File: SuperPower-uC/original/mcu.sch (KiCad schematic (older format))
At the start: 43 parts, among them J7 mcu_pinout, J8 mcu_pinout, Q7 S8050, Q8 S8050, U6 CP2102N-A01-GQFN28, U7 ESP32-WROOM32

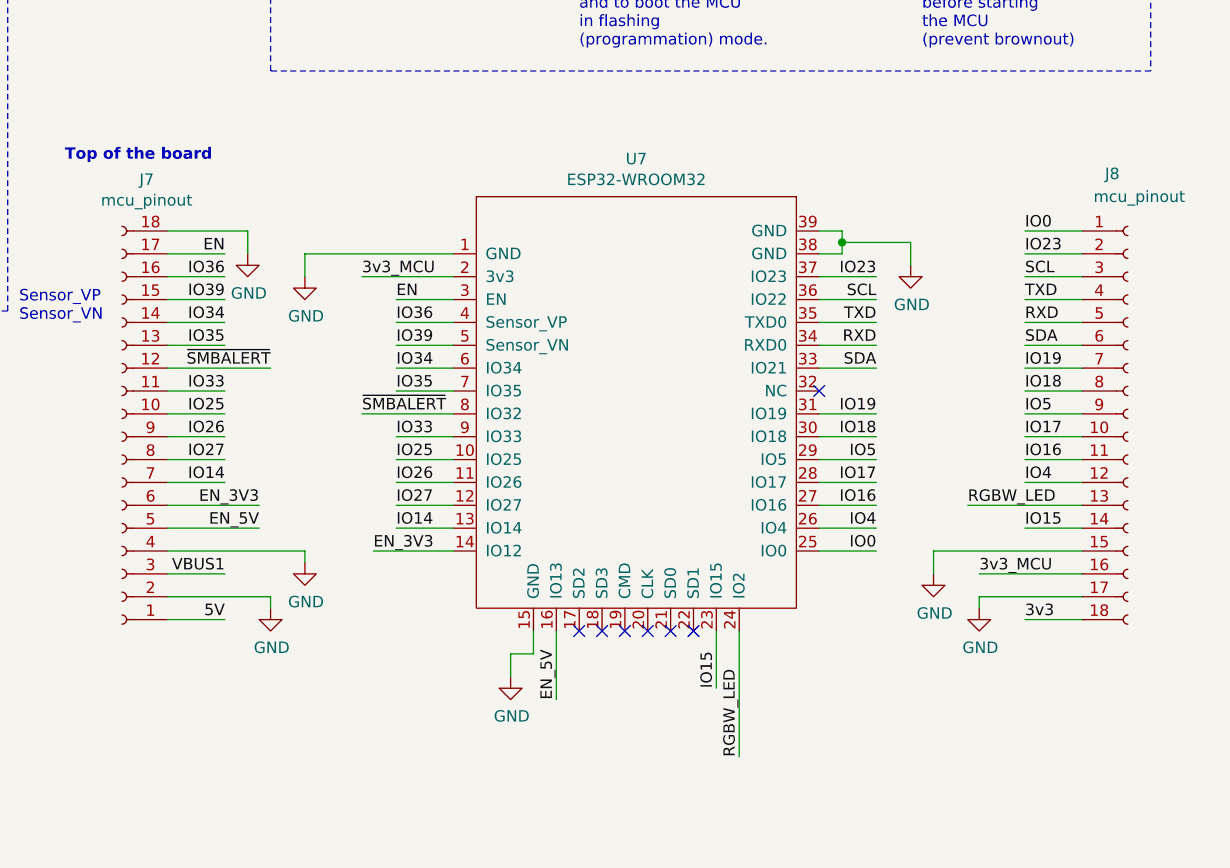
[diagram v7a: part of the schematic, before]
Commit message: Added additional 5+ amd 3.3+ - swapped VBUS to other connector
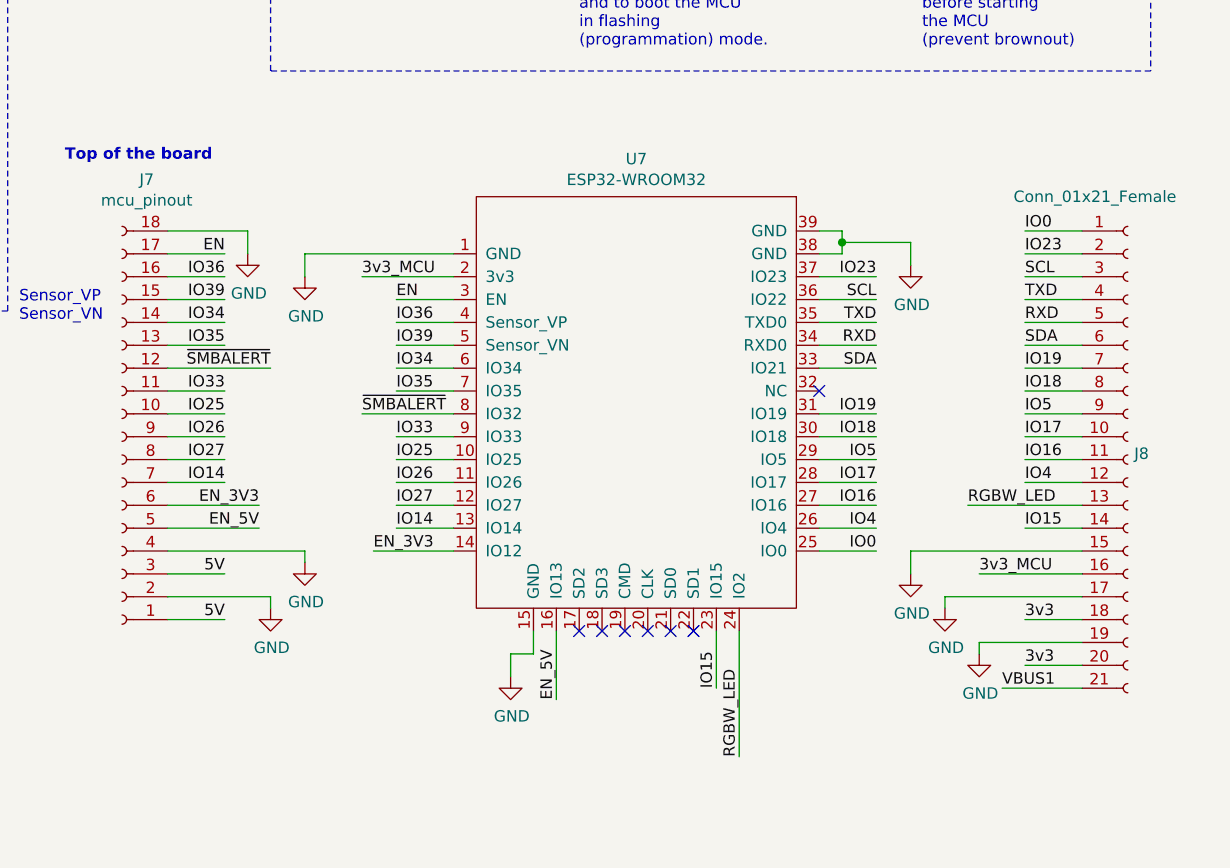
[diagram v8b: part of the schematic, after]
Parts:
- removed J8: mcu_pinout, Connector_PinSocket_2.54mm:PinSocket_1x18_P2.54mm_Vertical, symbol Connector:Conn_01x18_Female
- added J8: Conn_01x21_Female, Connector_PinSocket_2.54mm:PinSocket_1x21_P2.54mm_Vertical, symbol Connector:Conn_01x21_Female
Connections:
- net 3v3: now also J8.18 (Pin_18), J8.20 (Pin_20)
- net 3v3_MCU: now also J8.16 (Pin_16)
- net 5V: now also J7.3 (Pin_3)
- net GND: now also J8.15 (Pin_15), J8.17 (Pin_17), J8.19 (Pin_19)
- net IO0: now also J8.1 (Pin_1)
- net IO15: now also J8.14 (Pin_14)
- net IO16: now also J8.11 (Pin_11)
- net IO17: now also J8.10 (Pin_10)
- net IO18: now also J8.8 (Pin_8)
- net IO19: now also J8.7 (Pin_7)
- net IO23: now also J8.2 (Pin_2)
- net IO4: now also J8.12 (Pin_12)
- net IO5: now also J8.9 (Pin_9)
- net RGBW_LED: now also J8.13 (Pin_13)
- net RXD: now also J8.5 (Pin_5)
- net SCL: now also J8.3 (Pin_3)
- net SDA: now also J8.6 (Pin_6)
- net TXD: now also J8.4 (Pin_4)
- net VBUS1: now also J8.21 (Pin_21); no longer J7.3 (Pin_3)
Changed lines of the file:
@@
 L power:GND #PWR053
 U 1 1 5F8B01AA
-P 9750 5600
-F 0 "#PWR053" H 9750 5350 50  0001 C CNN
-F 1 "GND" H 9755 5427 50  0000 C CNN
-F 2 "" H 9750 5600 50  0001 C CNN
-F 3 "" H 9750 5600 50  0001 C CNN
-	1    9750 5600
-	1    0    0    -1
-$EndComp
-Wire Wire Line
-	9750 5600 9750 5500
+P 9650 5600
+F 0 "#PWR053" H 9650 5350 50  0001 C CNN
+F 1 "GND" H 9655 5427 50  0000 C CNN
+F 2 "" H 9650 5600 50  0001 C CNN
+F 3 "" H 9650 5600 50  0001 C CNN
+	1    9650 5600
+	1    0    0    -1
+$EndComp
 $Comp
 L power:PWR_FLAG #FLG?
@@
 Wire Wire Line
 	6400 5600 6650 5600
-Text Label 6650 5600 2    50   ~ 0
+Text Label 10050 6100 0    50   ~ 0
 VBUS1
 $Comp
@@
 Text Label 2050 1400 2    50   ~ 0
 3v3
-Wire Wire Line
-	9750 5500 10400 5500
 Text Label 6650 5800 2    50   ~ 0
 5V
@@
 	-1   0    0    1
 $EndComp
-$Comp
-L Connector:Conn_01x18_Female J8
-U 1 1 5FD07E44
-P 10600 4900
-F 0 "J8" H 10500 5950 50  0000 L CNN
-F 1 "mcu_pinout" H 10450 5850 50  0000 L CNN
-F 2 "Connector_PinSocket_2.54mm:PinSocket_1x18_P2.54mm_Vertical" H 10600 4900 50  0001 C CNN
-F 3 "~" H 10600 4900 50  0001 C CNN
-	1    10600 4900
-	1    0    0    -1
-$EndComp
 Wire Wire Line
 	10400 5800 10150 5800
@@
 L power:GND #PWR054
 U 1 1 5FD1F820
-P 9950 5750
-F 0 "#PWR054" H 9950 5500 50  0001 C CNN
-F 1 "GND" H 9955 5577 50  0000 C CNN
-F 2 "" H 9950 5750 50  0001 C CNN
-F 3 "" H 9950 5750 50  0001 C CNN
-	1    9950 5750
-	1    0    0    -1
-$EndComp
-Wire Wire Line
-	9950 5700 9950 5750
-Wire Wire Line
-	9950 5700 10400 5700
+P 9800 5750
+F 0 "#PWR054" H 9800 5500 50  0001 C CNN
+F 1 "GND" H 9805 5577 50  0000 C CNN
+F 2 "" H 9800 5750 50  0001 C CNN
+F 3 "" H 9800 5750 50  0001 C CNN
+	1    9800 5750
+	1    0    0    -1
+$EndComp
 Wire Wire Line
 	6850 5700 6850 5750
@@
 Wire Notes Line
 	2850 650  6250 650
+$Comp
+L Connector:Conn_01x21_Female J8
+U 1 1 5FEB7A5C
+P 10600 5100
+F 0 "J8" H 10628 5126 50  0000 L CNN
+F 1 "Conn_01x21_Female" H 10100 6250 50  0000 L CNN
+F 2 "Connector_PinSocket_2.54mm:PinSocket_1x21_P2.54mm_Vertical" H 10600 5100 50  0001 C CNN
+F 3 "~" H 10600 5100 50  0001 C CNN
+	1    10600 5100
+	1    0    0    -1
+$EndComp
+Text Label 10150 6000 0    50   ~ 0
+3v3
+$Comp
+L power:GND #PWR0108
+U 1 1 5FEBB004
+P 9950 5950
+F 0 "#PWR0108" H 9950 5700 50  0001 C CNN
+F 1 "GND" H 9955 5777 50  0000 C CNN
+F 2 "" H 9950 5950 50  0001 C CNN
+F 3 "" H 9950 5950 50  0001 C CNN
+	1    9950 5950
+	1    0    0    -1
+$EndComp
+Wire Wire Line
+	10400 6000 10150 6000
+Wire Wire Line
+	10400 6100 10050 6100
+Wire Wire Line
+	10400 5900 9950 5900
+Wire Wire Line
+	9950 5900 9950 5950
+Wire Wire Line
+	9800 5700 9800 5750
+Wire Wire Line
+	9650 5500 9650 5600
+Wire Wire Line
+	9650 5500 10400 5500
+Wire Wire Line
+	9800 5700 10400 5700
+Text Label 6650 5600 2    50   ~ 0
+5V
 $EndSCHEMATC
